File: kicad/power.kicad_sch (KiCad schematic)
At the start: 49 parts, among them J4 TYPE-C-31-M-12, Q7 BC847BW,115, U14 LD1117S33TR_SOT223, U15 MC34063AD, U16 MC34063AD

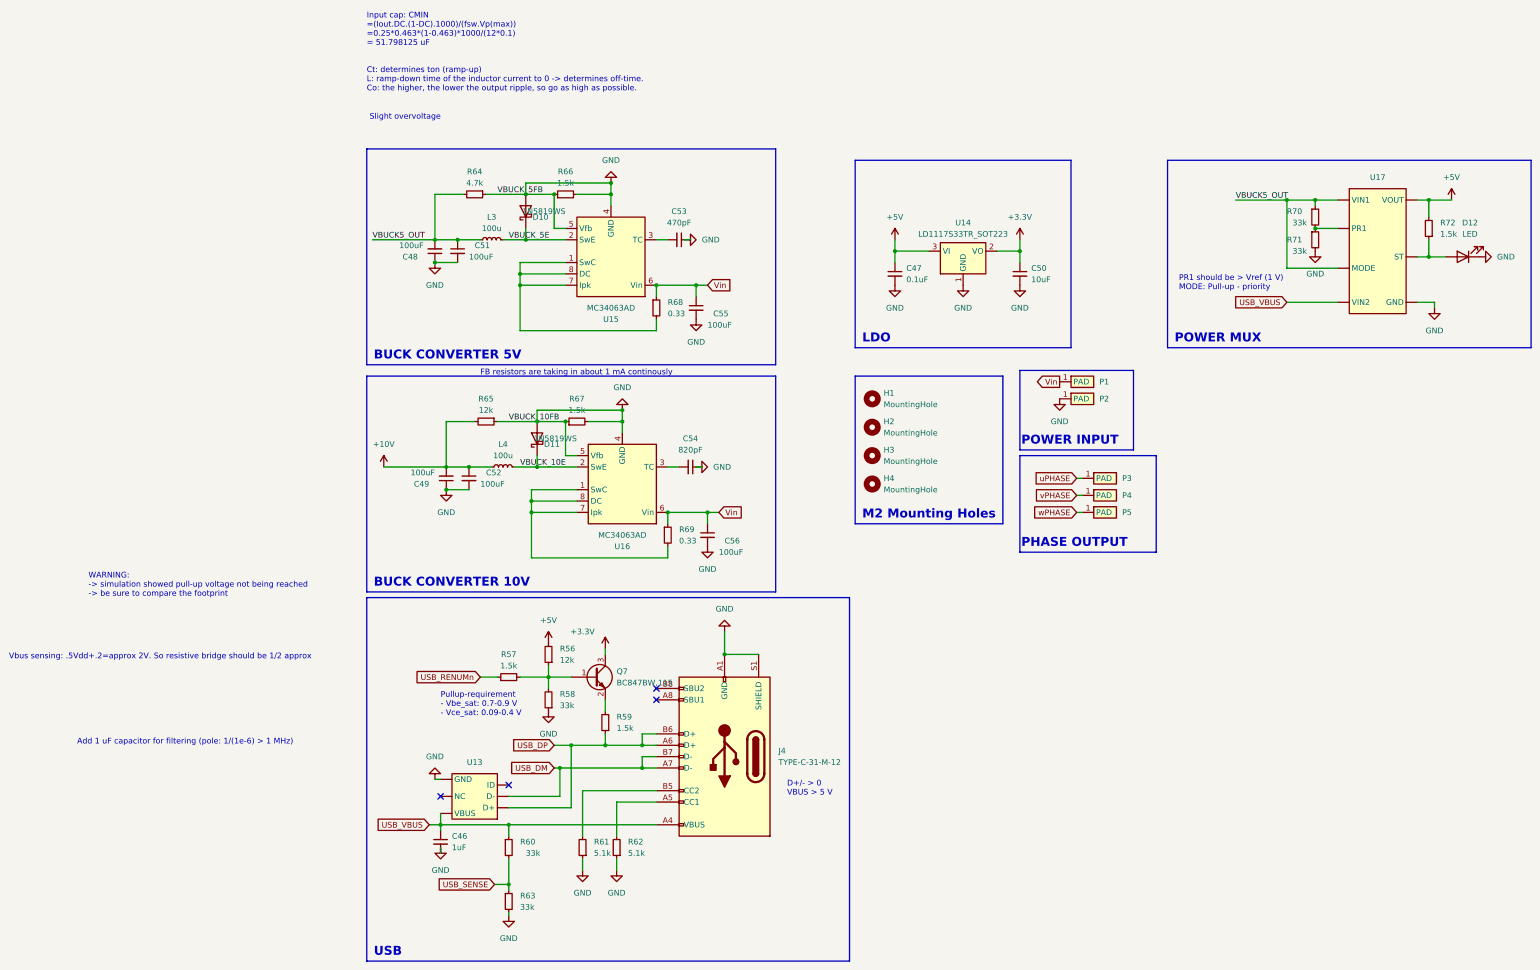
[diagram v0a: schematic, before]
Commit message: [kicad] added soldering pads for phases and battery connectors, rearranged schematic, added tooling holes, fixed ERC errors [scripts] minor footprint calculations
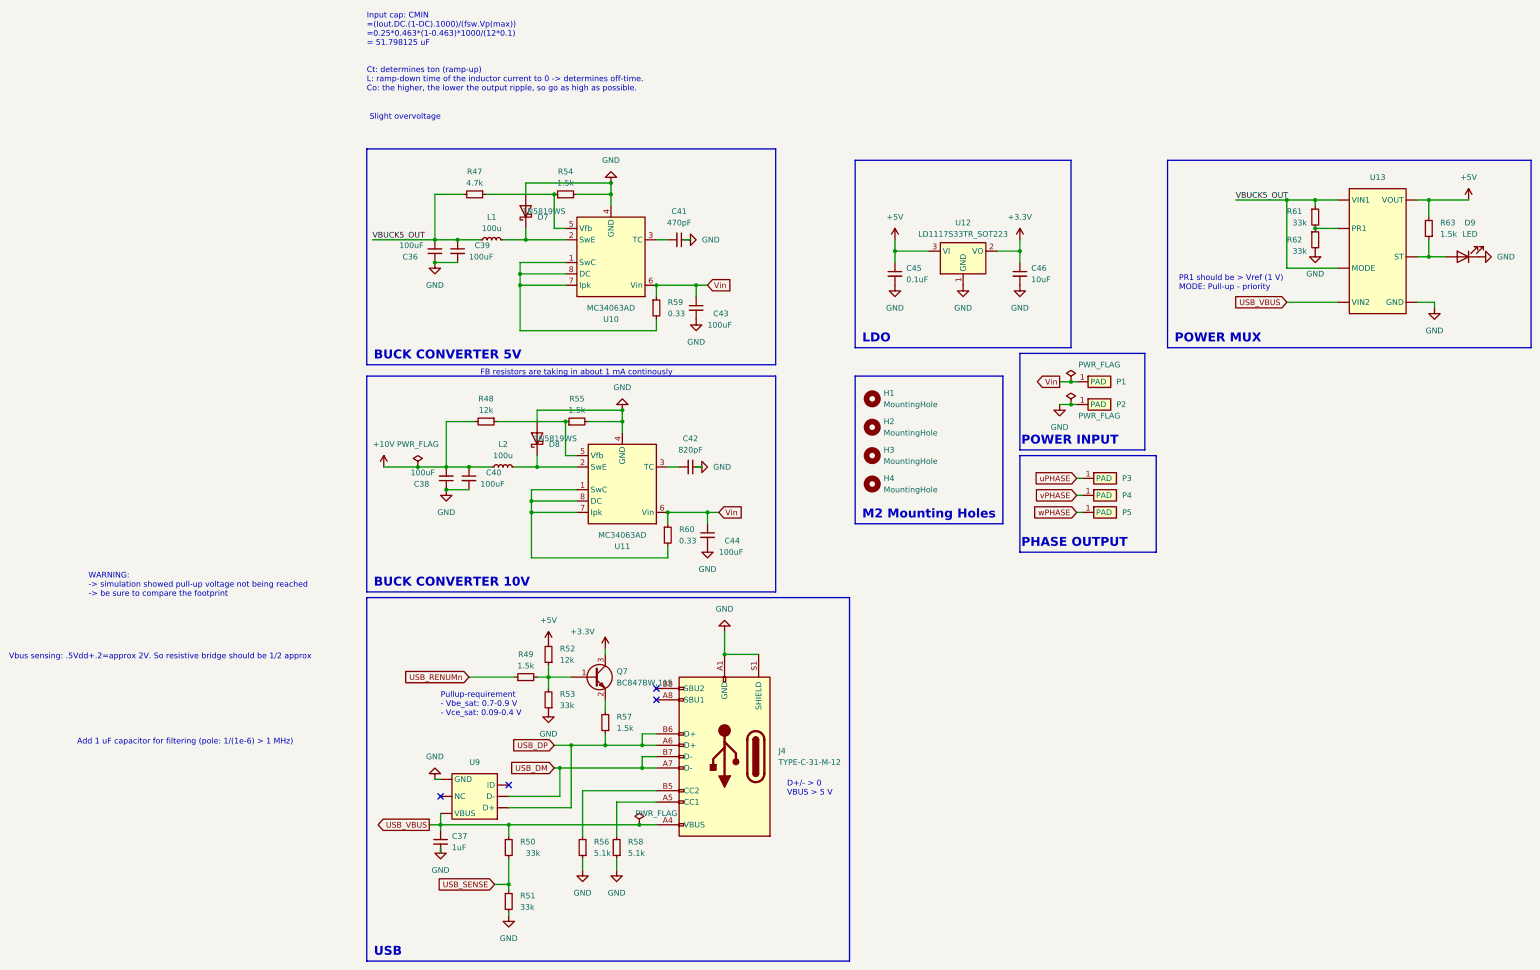
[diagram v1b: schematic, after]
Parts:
- renumbered C48 to C36, C46 to C37, C49 to C38, C51 to C39, C52 to C40, C53 to C41, C54 to C42, C55 to C43, C56 to C44, C47 to C45, C50 to C46, D10 to D7, D11 to D8, D12 to D9, L3 to L1, L4 to L2, R64 to R47, R65 to R48, R57 to R49, R60 to R50, R63 to R51, R56 to R52, R58 to R53, R66 to R54, R67 to R55, R61 to R56, R59 to R57, R62 to R58, R68 to R59, R69 to R60, R70 to R61, R71 to R62, R72 to R63, U15 to U10, U16 to U11, U14 to U12, U17 to U13, U13 to U9
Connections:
- net GND: no longer R47.1, R48.1, R54.1, R55.1, U10.5 (Vfb), U11.5 (Vfb)
- net VBUCK_10E: no longer names the net of D8.1 (K), L2.2, U11.2 (SwE)
- net VBUCK_5E: no longer names the net of D7.1 (K), L1.2, U10.2 (SwE)
- new net: R47.1, R54.1, U10.5 (Vfb)
- new net: R48.1, R55.1, U11.5 (Vfb)
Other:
- company: (none) -> Igor Wolfs
- title: (none) -> BLDC Driver Project
- moved on the sheet: P1, P2, R49

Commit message: [bldc] Fixed footprint issues, added jlcpcb man. rules, stackup decisions, added nets..
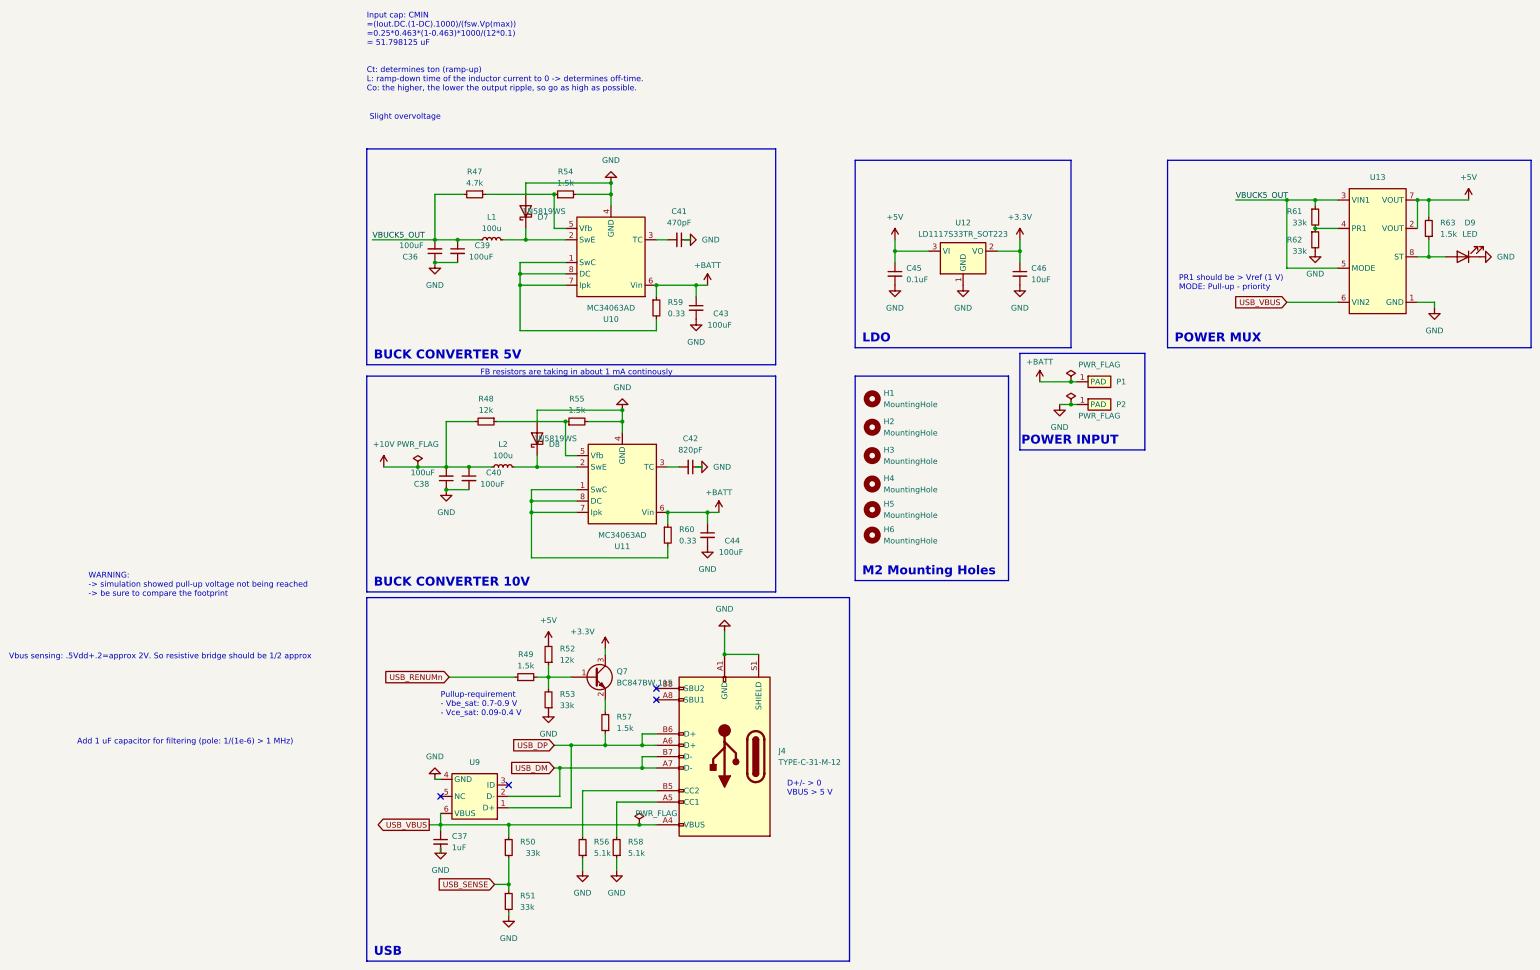
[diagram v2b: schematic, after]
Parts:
- removed P3, P4, P5: ~, bldc:SolderWirePad_1x01_SMD_5x10mm, symbol bldc:pad
- added H5, H6: MountingHole, MountingHole:MountingHole_3.2mm_M3_ISO14580, symbol Mechanical:MountingHole
- H1, H2, H3, H4: footprint MountingHole:MountingHole_2.1mm -> MountingHole:MountingHole_3.2mm_M3_ISO14580
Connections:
- net +5V: now also U13.2 (VOUT), U13.7 (VOUT); no longer U13. (VOUT)
- net GND: now also U13.1 (GND), U9.4 (GND); no longer U13. (VOUT), U9. (VBUS)
- net USB_DM: now also U9.2 (D-); no longer U9. (VBUS)
- net USB_DP: now also U9.1 (D+); no longer U9. (VBUS)
- net USB_VBUS: now also U13.6 (VIN2), U9.6 (VBUS); no longer U13. (VOUT), U9. (VBUS)
- net VBUCK5_OUT: now also U13.3 (VIN1), U13.5 (MODE); no longer U13. (VOUT)
- net at R61.2, R62.1: now also U13.4 (PR1); no longer U13. (VOUT)
- net at D9.2 (A), R63.1: now also U13.8 (ST); no longer U13. (VOUT)
- net Vin renamed +BATT

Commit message: [kicad] basic placement of everything but power and inverter, changed the ldo, changed caps
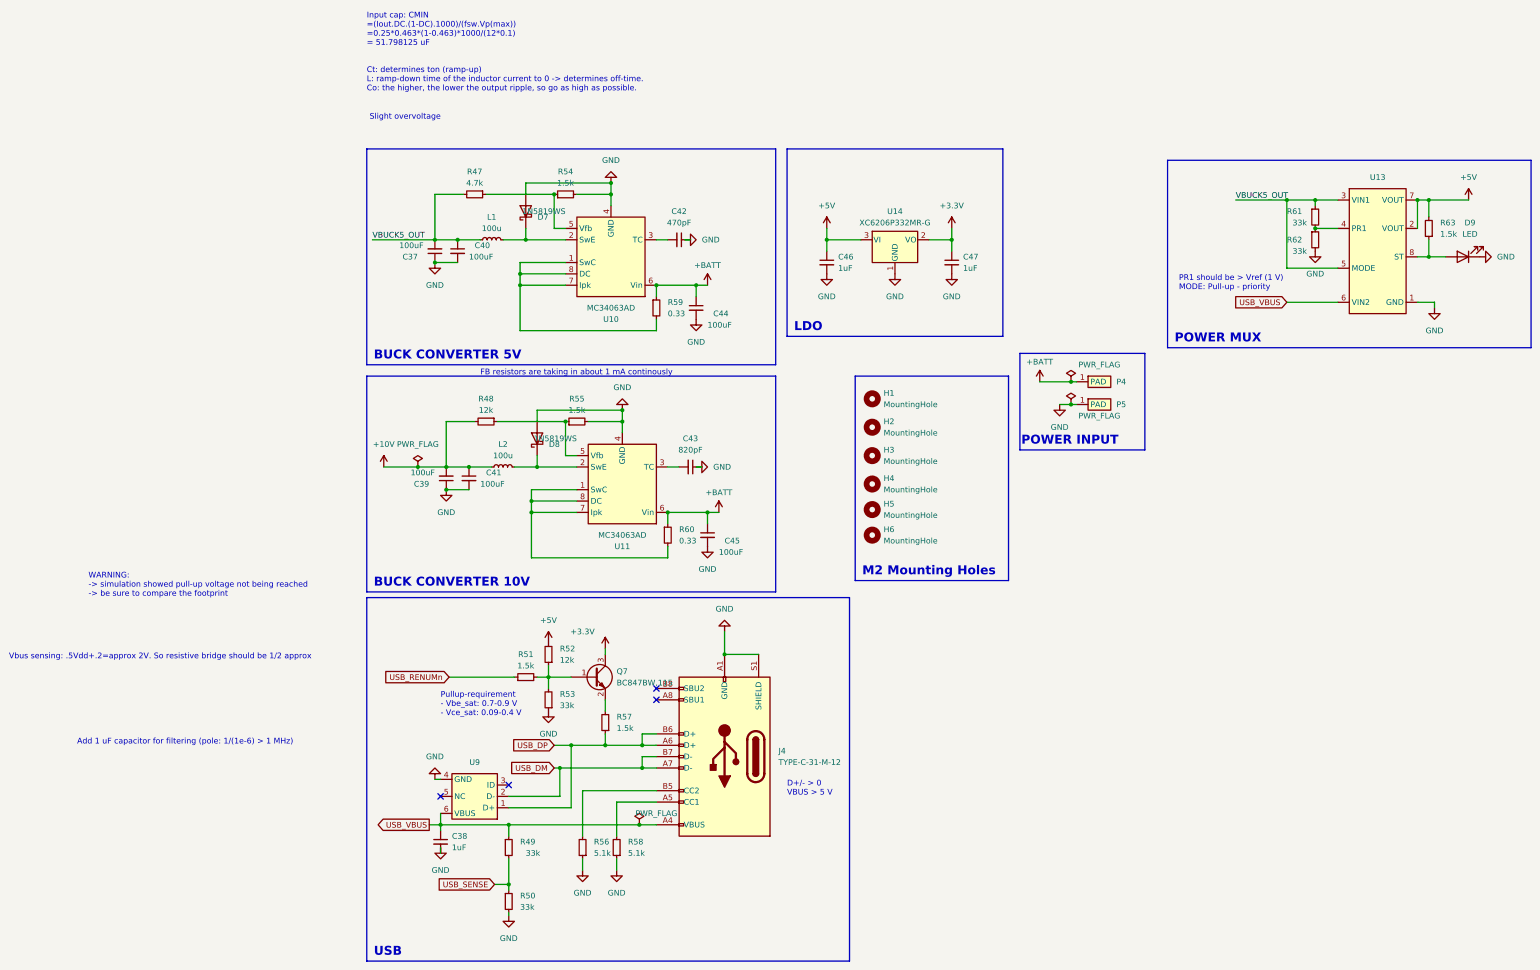
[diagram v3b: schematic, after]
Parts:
- removed C45: 0.1uF, Resistor_SMD:R_0402_1005Metric, symbol Device:C_Small
- removed U12: LD1117S33TR_SOT223, Package_TO_SOT_SMD:SOT-223-3_TabPin2, symbol Regulator_Linear:LD1117S33TR_SOT223
- added C47: 1uF, Capacitor_SMD:C_1206_3216Metric, symbol Device:C_Small
- added U14: XC6206P332MR-G, Package_TO_SOT_SMD:SOT-23, symbol Regulator_Linear:XC6206PxxxMR
- C46: value 10uF -> 1uF; footprint Capacitor_SMD:C_0402_1005Metric -> Capacitor_SMD:C_1206_3216Metric; MFR.Part (none) -> CL31B105KBHNNNE; jlcpcb C15525 -> C1848
- renumbered C36 to C37, C37 to C38, C38 to C39, C39 to C40, C40 to C41, C41 to C42, C42 to C43, C43 to C44, C44 to C45, P1 to P4, P2 to P5, R50 to R49, R51 to R50, R49 to R51
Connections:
- net +3.3V: now also C47.1, U14.2 (VO); no longer C46.1
- net +5V: now also C46.1, U14.3 (VI)
- net GND: now also C47.2, U14.1 (GND)

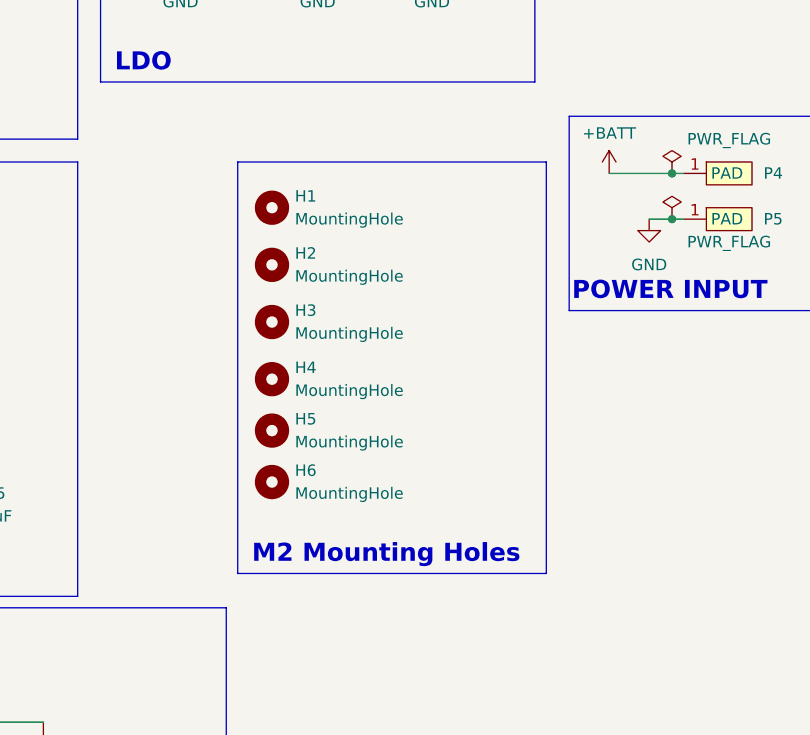
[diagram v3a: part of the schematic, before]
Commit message: [kicad] Changed mounting hole to jlcpcb type, poured 2 gnd layers, started with traces.
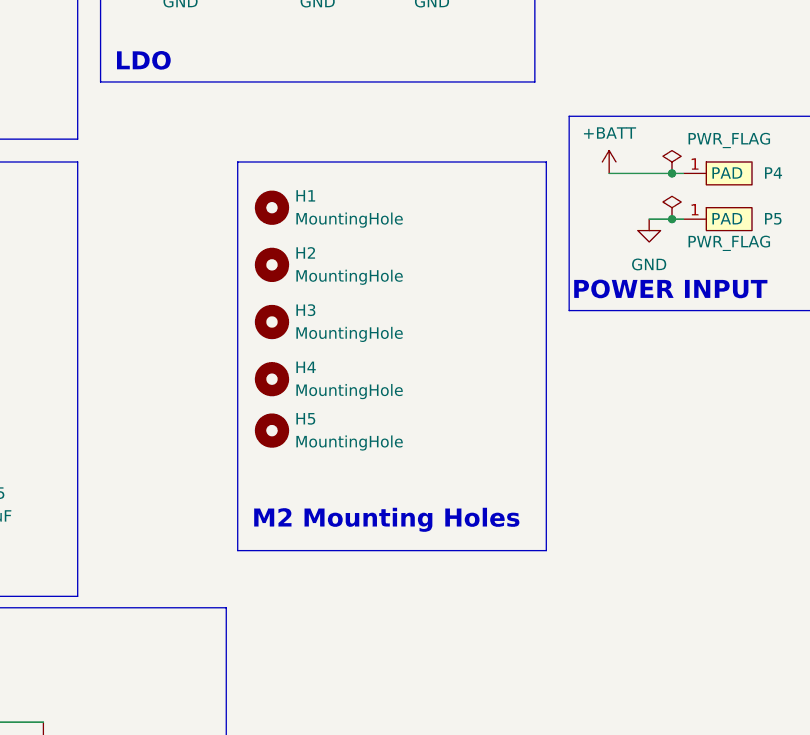
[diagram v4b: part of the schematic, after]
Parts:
- removed H3: MountingHole, MountingHole:MountingHole_3.2mm_M3_ISO14580, symbol Mechanical:MountingHole
- H1, H2, H4, H5: footprint MountingHole:MountingHole_3.2mm_M3_ISO14580 -> bldc:MountingHole_1.152mm_jlcpcb
- H3: renamed from H6; footprint MountingHole:MountingHole_3.2mm_M3_ISO14580 -> bldc:MountingHole_1.152mm_jlcpcb
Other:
- moved on the sheet: H3
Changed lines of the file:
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@@
     (fill (type none))
   )
-  (rectangle (start 124.46 64.77) (end 158.75 110.49)
+  (rectangle (start 124.46 64.77) (end 158.75 107.95)
     (stroke (width 0) (type default))
     (fill (type none))
@@
   )
   (text_box "M2 Mounting Holes"
-    (at 124.46 105.41 0) (size 34.29 5.08)
+    (at 124.46 101.6 0) (size 34.29 5.08)
     (stroke (width -0.0001) (type default))
     (fill (type none))
@@
     )
   )
-  (symbol (lib_id "Mechanical:MountingHole") (at 128.27 82.55 0) (unit 1)
-    (in_bom yes) (on_board yes) (dnp no) (fields_autoplaced)
-    (property "Reference" "H3" (at 130.81 81.28 0)
-      (effects (font (size 1.27 1.27)) (justify left))
-    )
-    (property "Value" "MountingHole" (at 130.81 83.82 0)
-      (effects (font (size 1.27 1.27)) (justify left))
-    )
-    (property "Footprint" "MountingHole:MountingHole_3.2mm_M3_ISO14580" (at 128.27 82.55 0)
-      (effects (font (size 1.27 1.27)) hide)
-    )
-    (property "Datasheet" "~" (at 128.27 82.55 0)
-      (effects (font (size 1.27 1.27)) hide)
-    )
-    (instances
-      (project "bldc_project"
-        (path "/91e2f46a-700b-4d7a-a06a-22469f63223f/53dc30ee-9af6-4771-8676-c78726df5d90"
-          (reference "H3") (unit 1)
-        )
-      )
-    )
-  )
   (symbol (lib_id "Regulator_Linear:XC6206PxxxMR") (at 133.35 34.29 0) (unit 1)
     (in_bom yes) (on_board yes) (dnp no) (fields_autoplaced)
@@
       (effects (font (size 1.27 1.27)) (justify left))
     )
-    (property "Footprint" "MountingHole:MountingHole_3.2mm_M3_ISO14580" (at 128.27 76.2 0)
+    (property "Footprint" "bldc:MountingHole_1.152mm_jlcpcb" (at 128.27 76.2 0)
       (effects (font (size 1.27 1.27)) hide)
     )
@@
       (effects (font (size 1.27 1.27)) (justify left))
     )
-    (property "Footprint" "MountingHole:MountingHole_3.2mm_M3_ISO14580" (at 128.27 69.85 0)
+    (property "Footprint" "bldc:MountingHole_1.152mm_jlcpcb" (at 128.27 69.85 0)
       (effects (font (size 1.27 1.27)) hide)
     )
@@
     )
   )
-  (symbol (lib_id "Mechanical:MountingHole") (at 128.27 100.33 0) (unit 1)
-    (in_bom yes) (on_board yes) (dnp no) (fields_autoplaced)
-    (property "Reference" "H6" (at 130.81 99.06 0)
-      (effects (font (size 1.27 1.27)) (justify left))
-    )
-    (property "Value" "MountingHole" (at 130.81 101.6 0)
-      (effects (font (size 1.27 1.27)) (justify left))
-    )
-    (property "Footprint" "MountingHole:MountingHole_3.2mm_M3_ISO14580" (at 128.27 100.33 0)
-      (effects (font (size 1.27 1.27)) hide)
-    )
-    (property "Datasheet" "~" (at 128.27 100.33 0)
-      (effects (font (size 1.27 1.27)) hide)
-    )
-    (instances
-      (project "bldc_project"
-        (path "/91e2f46a-700b-4d7a-a06a-22469f63223f/53dc30ee-9af6-4771-8676-c78726df5d90"
-          (reference "H6") (unit 1)
+  (symbol (lib_id "Mechanical:MountingHole") (at 128.27 82.55 0) (unit 1)
+    (in_bom yes) (on_board yes) (dnp no) (fields_autoplaced)
+    (property "Reference" "H3" (at 130.81 81.28 0)
+      (effects (font (size 1.27 1.27)) (justify left))
+    )
+    (property "Value" "MountingHole" (at 130.81 83.82 0)
+      (effects (font (size 1.27 1.27)) (justify left))
+    )
+    (property "Footprint" "bldc:MountingHole_1.152mm_jlcpcb" (at 128.27 82.55 0)
+      (effects (font (size 1.27 1.27)) hide)
+    )
+    (property "Datasheet" "~" (at 128.27 82.55 0)
+      (effects (font (size 1.27 1.27)) hide)
+    )
+    (instances
+      (project "bldc_project"
+        (path "/91e2f46a-700b-4d7a-a06a-22469f63223f/53dc30ee-9af6-4771-8676-c78726df5d90"
+          (reference "H3") (unit 1)
         )
       )
@@
       (effects (font (size 1.27 1.27)) (justify left))
     )
-    (property "Footprint" "MountingHole:MountingHole_3.2mm_M3_ISO14580" (at 128.27 94.615 0)
+    (property "Footprint" "bldc:MountingHole_1.152mm_jlcpcb" (at 128.27 94.615 0)
       (effects (font (size 1.27 1.27)) hide)
     )
@@
       (effects (font (size 1.27 1.27)) (justify left))
     )
-    (property "Footprint" "MountingHole:MountingHole_3.2mm_M3_ISO14580" (at 128.27 88.9 0)
-      (effects (font (size 1.27 1.27)) hide)
-    )
+    (property "Footprint" "bldc:MountingHole_1.152mm_jlcpcb" (at 128.27 88.9 0)
+      (effects (font (size 1.27 1.27)) hide)
+    )
